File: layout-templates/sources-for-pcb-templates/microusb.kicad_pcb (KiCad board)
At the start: 2 copper layers, 14 x 5.2 mm, 9 parts

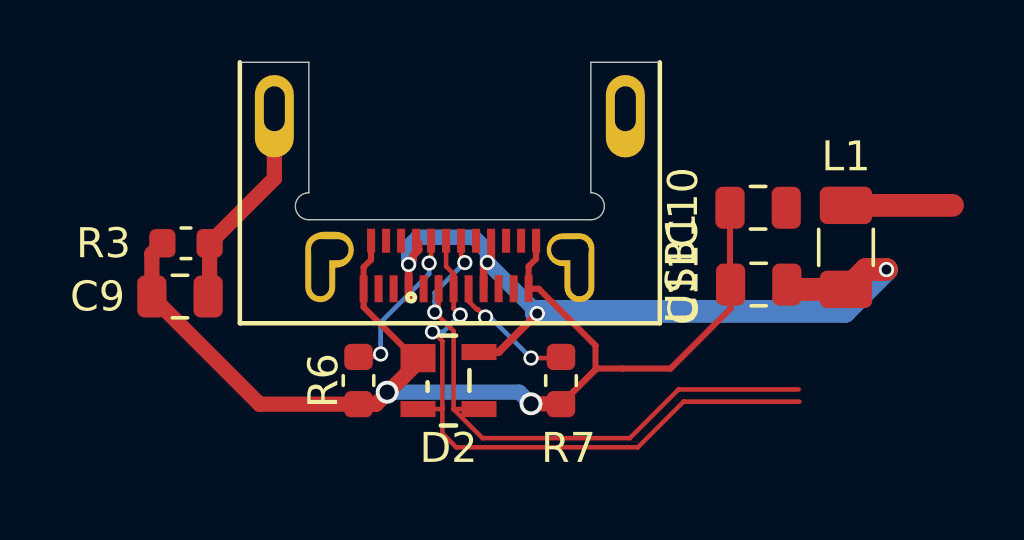
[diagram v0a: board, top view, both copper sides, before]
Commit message: Trying to get back to Kicad 5.1 compat and fix USB routing
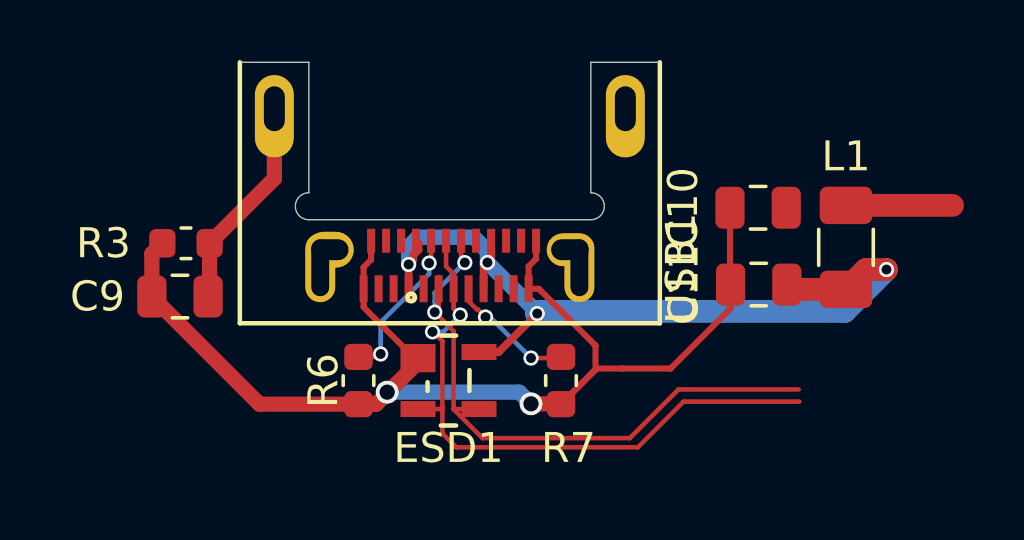
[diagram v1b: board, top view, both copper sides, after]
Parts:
- renumbered D2 to ESD1
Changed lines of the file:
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@@
   (module "Keyboardio:PRTR5V0U2X" (layer "F.Cu")
     (at 32.26 -67.7803 270)
-    (fp_text reference "D2" (at 2.25 0) (layer "F.SilkS")
+    (fp_text reference "ESD1" (at 2.25 0) (layer "F.SilkS")
       (effects (font (size 1 1) (thickness 0.15)))
     )
